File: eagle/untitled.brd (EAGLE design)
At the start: 55.8 x 50.8 mm, 34 parts, among them Q1 IRFZ24NPBF, U1 ATTINY85-20S, X1 MKDSN1,5/3-5,08, X2 MKDSN1,5/3-5,08

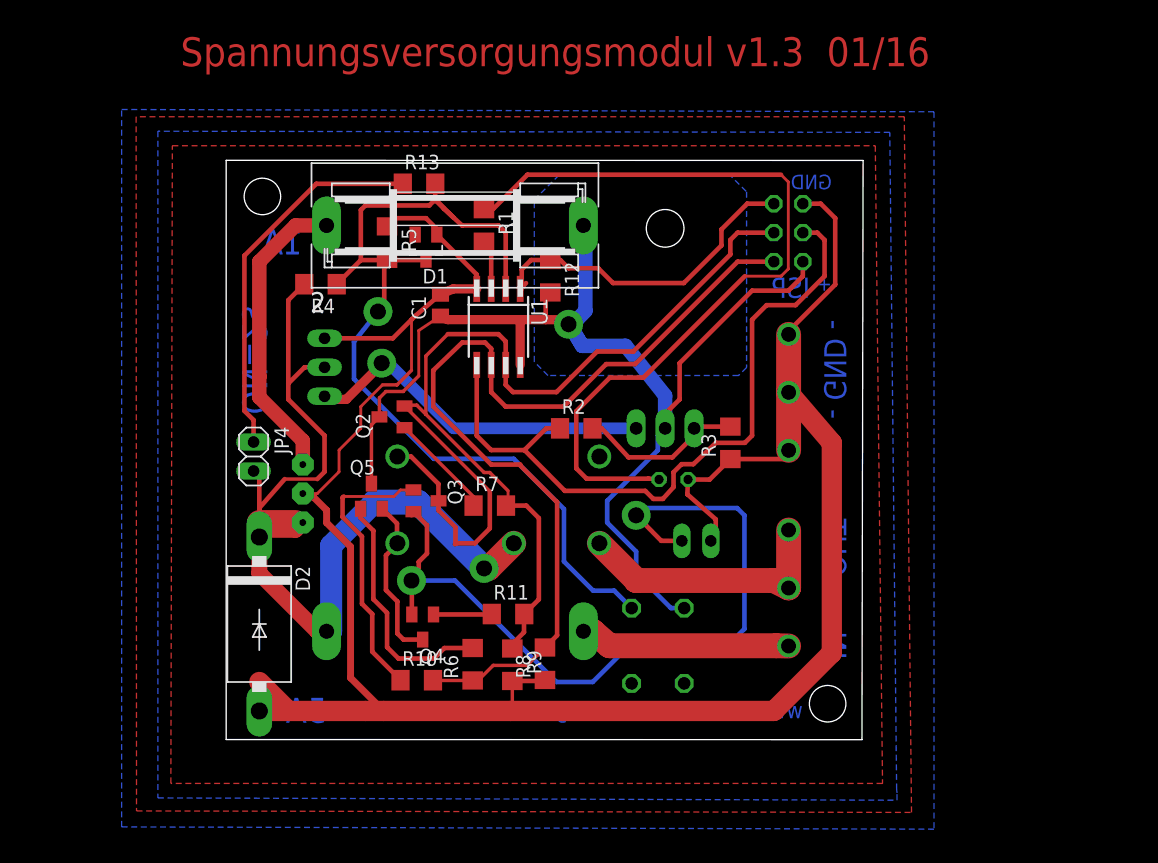
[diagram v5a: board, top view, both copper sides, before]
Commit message: Updated to version 2.1 with mosfets instead of a relay
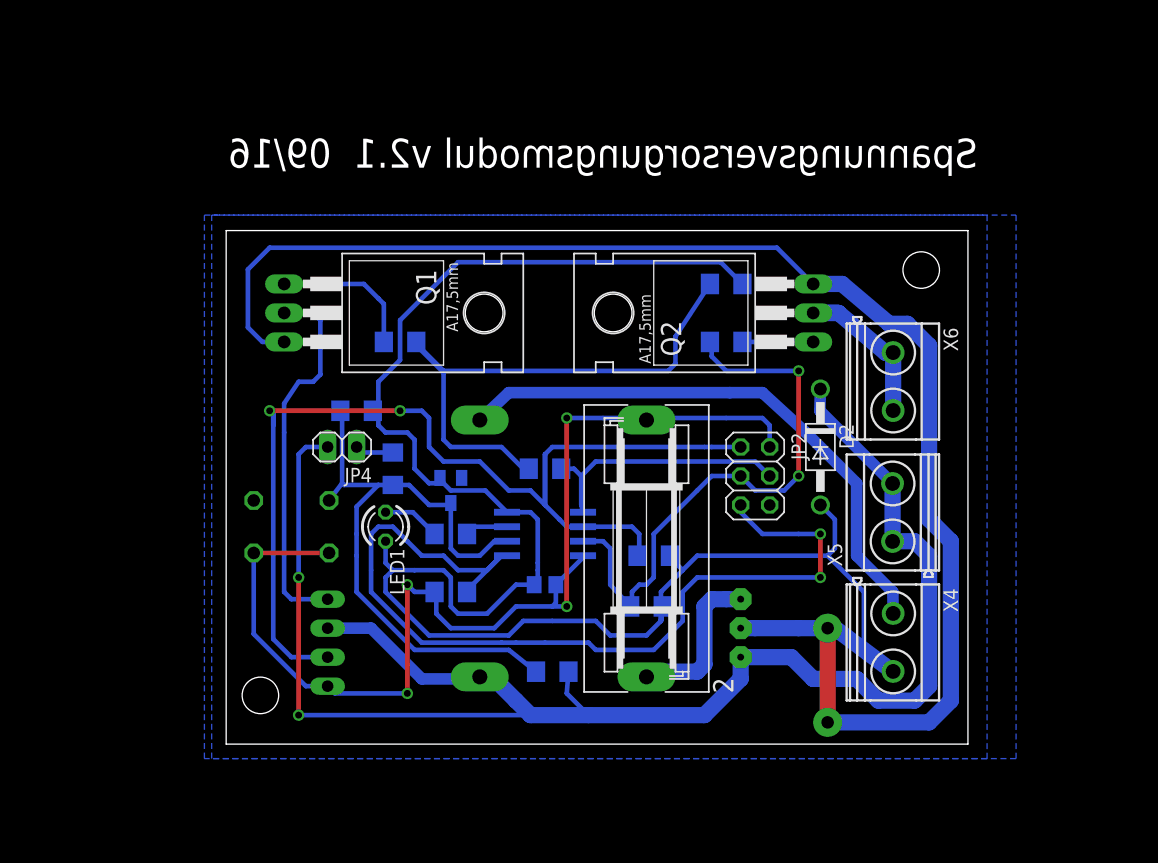
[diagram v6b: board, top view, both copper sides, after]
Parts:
- removed JP3: (no value), pinhead:1X02
- removed Q3, Q4, Q5: (no value), semicon-smd-ipc:SOT23
- removed R10, R11: 6,8k, rcl:R1206
- removed U$2: TRS-1BISTABIL-SCHRACK, 0liver:PRINTRELAIS-SCHRACK-PE-BISTABIL
- removed X1, X2: MKDSN1,5/3-5,08, con-phoenix-508:MKDSN1,5/3-5,08
- added X4, X5, X6: MKDSN1,5/2-5,08, con-phoenix-508:MKDSN1,5/2-5,08
- D2: value (none) -> 1N4004; device diode:DO201-15 -> diode:DO41-10
- JP1: device pinhead:1X03 -> pinhead:1X04
- Q1: value IRFZ24NPBF -> IRLZ34N
- Q2: value (none) -> IRLZ34N; device semicon-smd-ipc:SOT23 -> 0liver:TO220BH
- R1: value 220 -> 150
- R6: value 6,8k -> 100
- R7: value 6,8k -> 0
- R8: value 200k -> 10k
- R9: value 200k -> 100k
- moved D2 51.6 mm to (52.1, 26.0)
- moved U$1 40.1 mm to (45.1, 7.62)
- moved R4 39.6 mm to (28.6, 6.35), flipped to the bottom
- moved R6 35.9 mm to (43.8, 35.2), flipped to the bottom, turned to 0 degrees
- moved S1 33.8 mm to (5.71, 19.1), turned to 180 degrees
- moved 2 32.9 mm to (36.8, 17.1), turned to 90 degrees
- moved Q2 31.9 mm to (45.1, 37.8)
- moved R12 29.0 mm to (19.7, 13.3), flipped to the bottom, turned to 0 degrees
- moved Q1 27.3 mm to (11.4, 37.8), flipped to the top, turned to 270 degrees
- moved R1 27.2 mm to (19.7, 18.4), flipped to the bottom, turned to 180 degrees
- moved C1 26.2 mm to (27.9, 14.0), flipped to the bottom, turned to 0 degrees
- moved LED1 25.6 mm to (14.0, 19.1), flipped to the top, turned to 270 degrees
- moved R13 25.1 mm to (14.6, 24.1), flipped to the bottom, turned to 270 degrees
- moved JP1 24.1 mm to (8.89, 8.89)
- moved JP2 21.5 mm to (46.4, 23.5), flipped to the top, turned to 270 degrees
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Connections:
- removed net N$11: Q2.2, Q3.3, U$2.P$1
- removed net N$13: Q4.3, Q5.2, U$2.P$2
- removed net N$14: Q5.1, R6.2
- removed net N$15: Q2.1, R7.1
- removed net N$17: U$2.P$4, X1.2, X1.3
- removed net N$19: Q3.1, R10.1
- removed net N$20: Q4.1, R11.1
- removed net N$9: JP1.1, Q1.S
- new net N$21: JP1.4, Q1.D
- new net N$3: Q2.D, X6.1, X6.2
- new net N$7: Q1.G, R7.1
- net +5V: now also JP1.1; no longer Q1.D, Q2.3, Q5.3
- net GND: now also Q1.S, Q2.S, X4.2; no longer JP1.3, JP3.2, X2.1, X2.2, X2.3
- net MISO: now also JP1.2; no longer R10.2, R6.1
- net N$1: now also X4.1; no longer X1.1
- net N$2: now also JP1.3, X5.1, X5.2; no longer JP1.2, U$2.P$3
- net N$4: now also Q2.G, R6.1; no longer JP3.1, Q3.2, Q4.2
- net N$8: now also R7.2; no longer Q1.G
- net SCK: now also R6.2; no longer R11.2, R7.2
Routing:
- net GND: track 199.8 -> 300.9 mm, vias 0 -> 2
- net N$6: track 73.2 -> 5.23 mm
- net N$4: track 70.1 -> 6.20 mm, vias 2 -> 0
- net N$2: track 85.3 -> 145.6 mm, vias 1 -> 2
- net N$10: track 29.5 -> 82.3 mm, vias 0 -> 2
- net MOSI: track 63.0 -> 25.3 mm
- net N$8: track 14.7 -> 50.4 mm
- net N$21: track 0.00 -> 33.2 mm
- net N$9: track 32.7 -> 0.00 mm, vias 1 -> 0
- net N$1: track 18.5 -> 49.9 mm
- net N$16: track 33.1 -> 3.38 mm
- net N$11: track 28.1 -> 0.00 mm
- net SCK: track 76.9 -> 50.6 mm, vias 0 -> 2
- net RESET: track 83.6 -> 57.6 mm, vias 1 -> 0
- net N$19: track 24.6 -> 0.00 mm
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- added copper zone on layer 16, net N$5
- removed copper zone on layer 16, net +5V
- removed copper zone on layer 1, net GND
- removed copper zone on layer 1, net N$5
- removed copper zone on layer 16, net N$7
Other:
- board size 55.8 x 50.8 mm -> 65 x 45 mm
- board text added: "Spannungsversorgungsmodul v2.1 09/16"
- board text removed: "+"
- board text removed: "- GND -"
- board text removed: "-OUT-"
- board text removed: "1A"
- board text removed: "5A"
- board text removed: "GND"
- board text removed: "IN"
- board text removed: "ISP"
- board text removed: "ON=2s"
- board text removed: "Spannungsversorgungsmodul v1.3 01/16"
- board text removed: "www.tief-dunkel-kalt.org 01/16 V1.3"
